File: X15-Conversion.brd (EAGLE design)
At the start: 50.8 x 62.9 mm, 31 parts, among them U1 LINEAR,AZ1117CR-3.3TRG1DIODES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

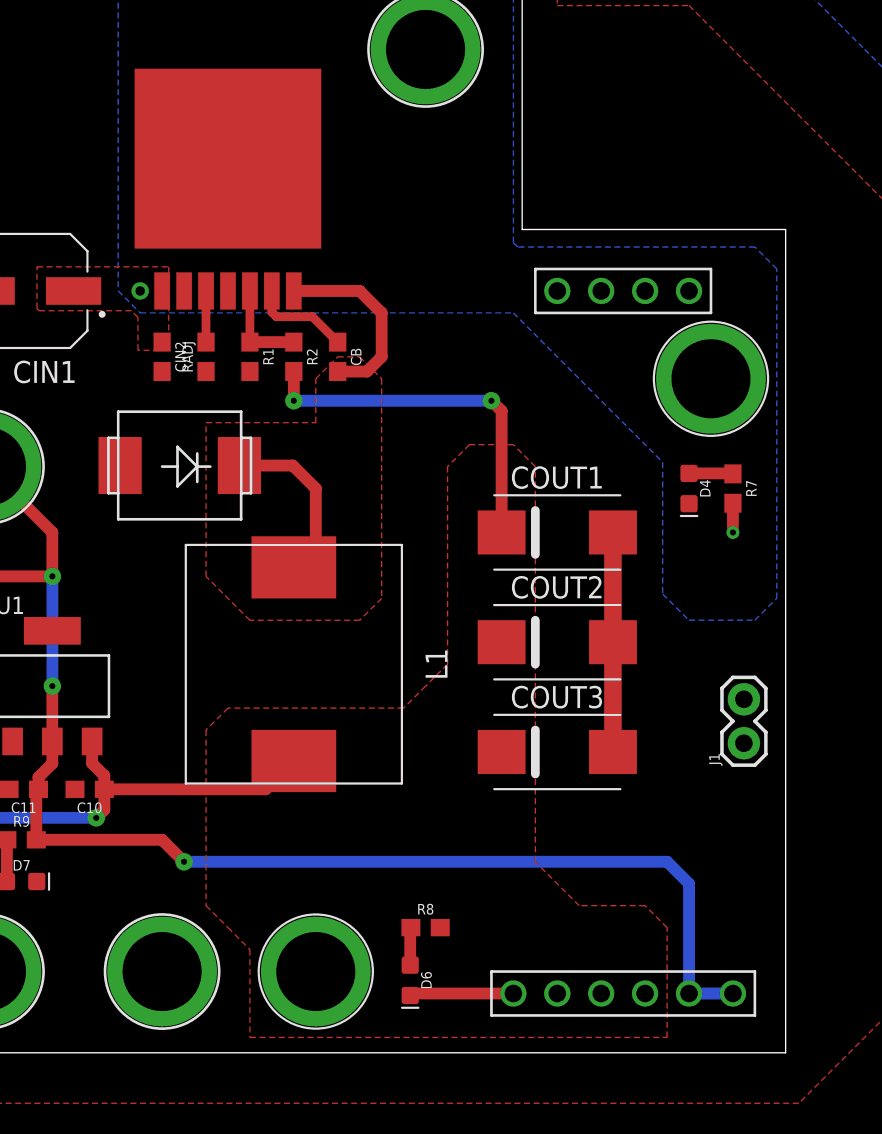
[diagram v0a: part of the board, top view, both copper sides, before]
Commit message: Changed the fonts
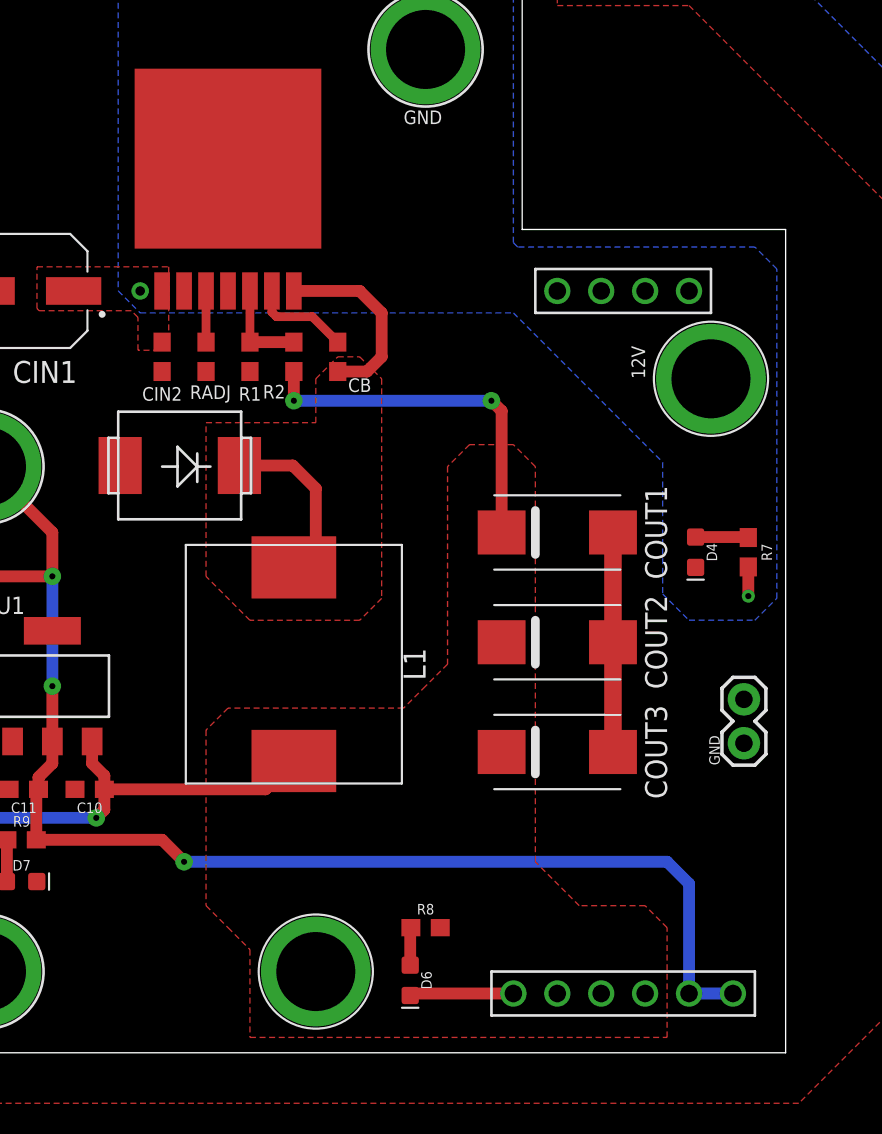
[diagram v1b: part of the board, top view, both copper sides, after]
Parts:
- removed U$13: GND_TESTPOINT, X15-Conversion-Parts-Library:GND_TESTPOINT
- moved U$11 10.2 mm to (5.08, 5.08)
- moved R7 3.79 mm to (49.1, 29.3)
- moved D4 3.70 mm to (46.1, 29.3)
- renumbered J1 to GND
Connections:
- net GND: no longer U$13.GND
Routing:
- net N$8: track 2.55 -> 3.06 mm
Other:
- board text added: "12V"
- board text added: "GND"

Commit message: Changed some wires
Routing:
- net BOOST: track 5.75 -> 6.35 mm
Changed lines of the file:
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@@
 <wire x1="11.899" y1="16.411" x2="11.19" y2="17.12" width="0.6858" layer="1"/>
 <wire x1="11.19" y1="17.12" x2="11.19" y2="18.39" width="0.6858" layer="1"/>
-<wire x1="11.899" y1="15.621" x2="21.221" y2="15.621" width="0.6858" layer="1"/>
-<wire x1="21.221" y1="15.621" x2="22.86" y2="17.26" width="0.6858" layer="1"/>
+<wire x1="22.491" y1="16.891" x2="15.709" y2="16.891" width="0.6858" layer="1"/>
+<wire x1="15.709" y1="16.891" x2="14.439" y2="15.621" width="0.6858" layer="1"/>
+<wire x1="14.439" y1="15.621" x2="11.899" y2="15.621" width="0.6858" layer="1"/>
+<wire x1="22.491" y1="16.891" x2="22.86" y2="17.26" width="0.6858" layer="1"/>
 <contactref element="J3" pad="2"/>
 <contactref element="J3" pad="1"/>
@@
 <contactref element="R9" pad="2"/>
 <contactref element="U1" pad="2"/>
-<wire x1="15.24" y1="12.7" x2="16.51" y2="11.43" width="0.6858" layer="1"/>
-<wire x1="15.24" y1="12.7" x2="7.962" y2="12.7" width="0.6858" layer="1"/>
+<wire x1="13.97" y1="11.43" x2="16.51" y2="11.43" width="0.6858" layer="1"/>
+<wire x1="13.97" y1="11.43" x2="12.7" y2="12.7" width="0.6858" layer="1"/>
+<wire x1="12.7" y1="12.7" x2="7.962" y2="12.7" width="0.6858" layer="1"/>
 <via x="16.51" y="11.43" extent="1-16" drill="0.35" diameter="1.016"/>
 <wire x1="16.51" y1="11.43" x2="44.45" y2="11.43" width="0.6858" layer="16"/>
@@
 <wire x1="21.59" y1="44.45" x2="21.59" y2="43.2292625" width="0.508" layer="1"/>
 <wire x1="21.8556625" y1="42.9636" x2="21.59" y2="43.2292625" width="0.508" layer="1"/>
-<wire x1="23.9264" y1="42.9636" x2="25.4" y2="41.49" width="0.508" layer="1"/>
-<wire x1="21.8556625" y1="42.9636" x2="23.9264" y2="42.9636" width="0.508" layer="1"/>
+<wire x1="25.4" y1="42.506" x2="24.9424" y2="42.9636" width="0.508" layer="1"/>
+<wire x1="25.4" y1="42.506" x2="25.4" y2="41.49" width="0.508" layer="1"/>
+<wire x1="21.8556625" y1="42.9636" x2="24.9424" y2="42.9636" width="0.508" layer="1"/>
 </signal>
 <signal name="FB">

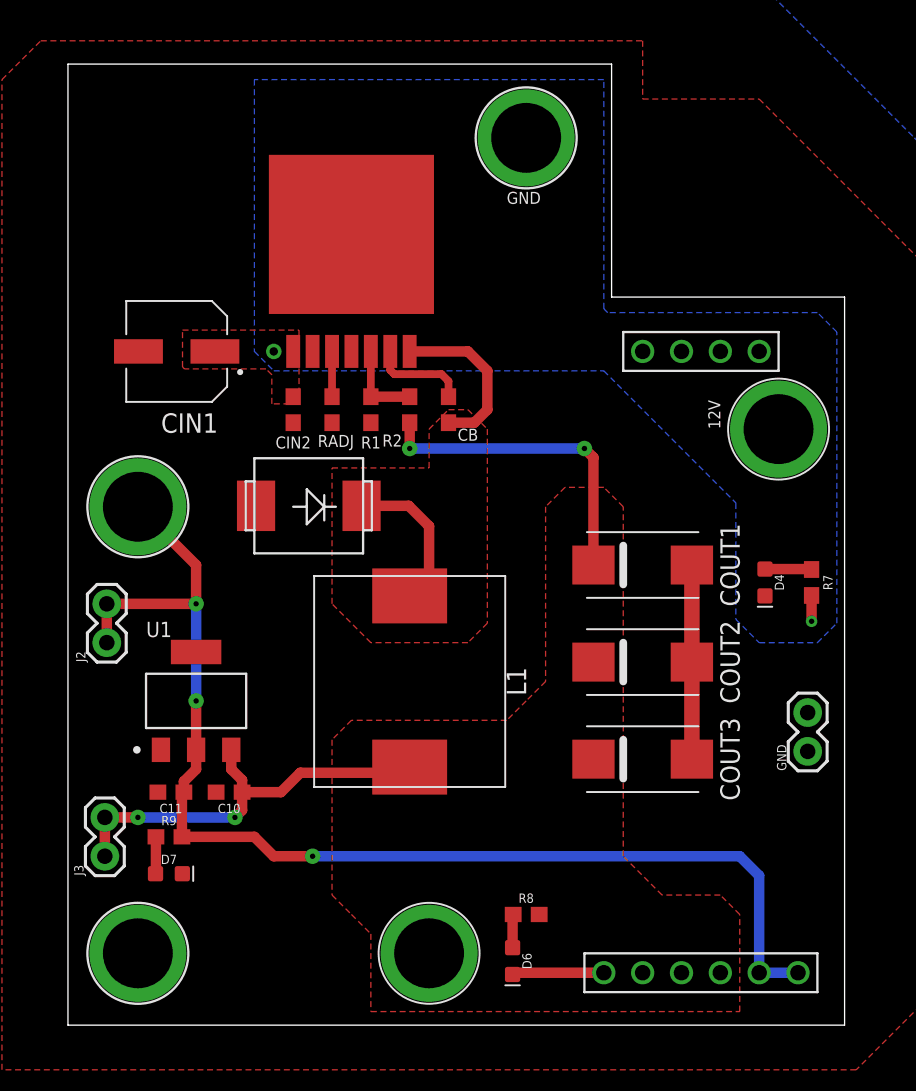
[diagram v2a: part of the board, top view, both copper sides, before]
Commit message: Added vias to ground
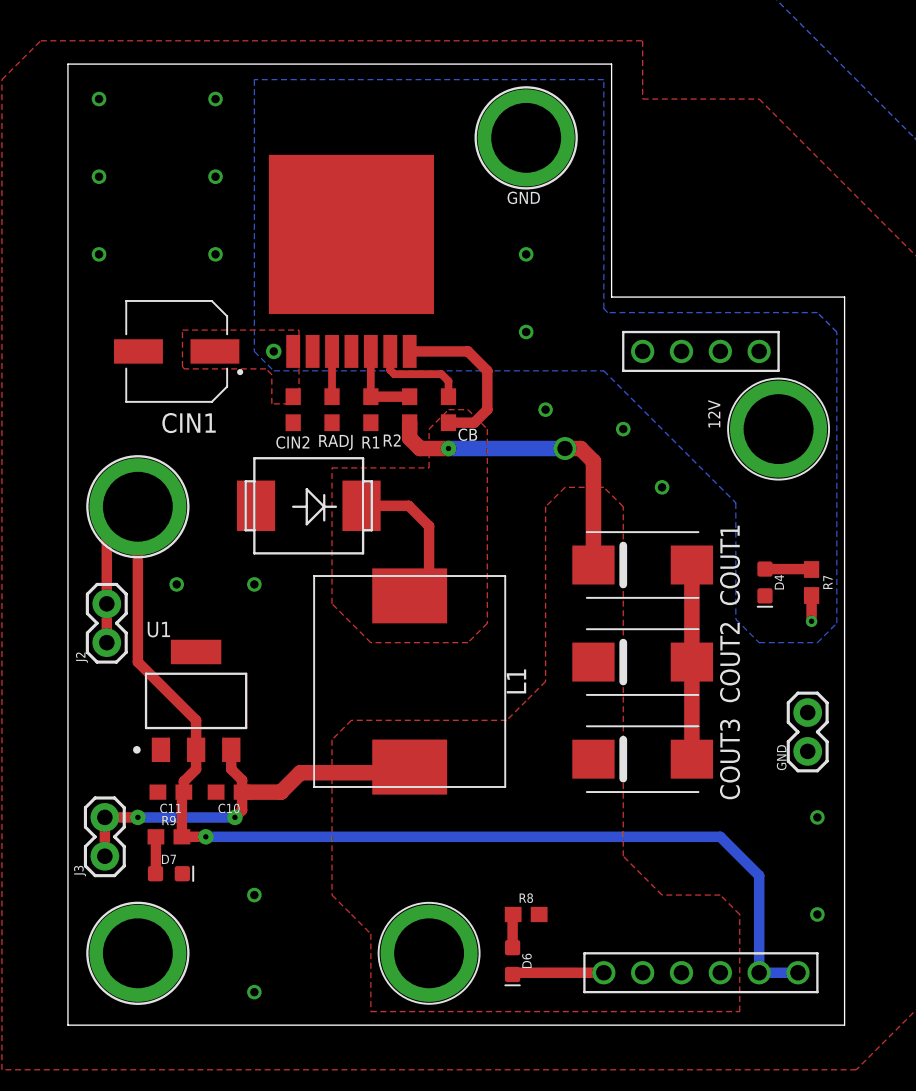
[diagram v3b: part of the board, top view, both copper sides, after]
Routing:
- net 3.3V: track 79.6 -> 81.0 mm, vias 3 -> 1
- net 5.2V: track 48.6 -> 48.0 mm
- net GND: vias 0 -> 17
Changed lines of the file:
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@@
 <vertex x="-10.16" y="63.5"/>
 </polygon>
+<via x="2.54" y="60.96" extent="1-16" drill="0.55"/>
+<via x="30.48" y="50.8" extent="1-16" drill="0.55"/>
+<via x="30.48" y="45.72" extent="1-16" drill="0.55"/>
+<via x="31.75" y="40.64" extent="1-16" drill="0.55"/>
+<via x="2.54" y="55.88" extent="1-16" drill="0.55"/>
+<via x="2.54" y="50.8" extent="1-16" drill="0.55"/>
+<via x="10.16" y="60.96" extent="1-16" drill="0.55"/>
+<via x="10.16" y="55.88" extent="1-16" drill="0.55"/>
+<via x="10.16" y="50.8" extent="1-16" drill="0.55"/>
+<via x="7.62" y="29.21" extent="1-16" drill="0.55"/>
+<via x="12.7" y="29.21" extent="1-16" drill="0.55"/>
+<via x="12.7" y="8.89" extent="1-16" drill="0.55"/>
+<via x="12.7" y="2.54" extent="1-16" drill="0.55"/>
+<via x="49.53" y="7.62" extent="1-16" drill="0.55"/>
+<via x="49.53" y="13.97" extent="1-16" drill="0.55"/>
+<via x="39.37" y="35.56" extent="1-16" drill="0.55"/>
+<via x="36.83" y="39.37" extent="1-16" drill="0.55"/>
 </signal>
 <signal name="5.2V">
@@
 <contactref element="COUT3" pad="+"/>
 <contactref element="L1" pad="2"/>
-<wire x1="34.88" y1="30.48" x2="34.88" y2="37.51" width="0.6858" layer="1"/>
-<wire x1="34.88" y1="37.51" x2="34.29" y2="38.1" width="0.6858" layer="1"/>
-<via x="34.29" y="38.1" extent="1-16" drill="0.35" diameter="1.016"/>
-<wire x1="22.86" y1="39.79" x2="22.86" y2="38.1" width="0.6858" layer="1"/>
-<via x="22.86" y="38.1" extent="1-16" drill="0.35" diameter="1.016"/>
-<wire x1="22.86" y1="38.1" x2="34.29" y2="38.1" width="0.6858" layer="16"/>
+<wire x1="34.88" y1="30.48" x2="34.88" y2="37.256" width="1.016" layer="1"/>
+<wire x1="34.88" y1="37.256" x2="34.036" y2="38.1" width="1.016" layer="1"/>
+<wire x1="34.036" y1="38.1" x2="33.02" y2="38.1" width="1.016" layer="1"/>
+<via x="33.02" y="38.1" extent="1-16" drill="1" diameter="1.016"/>
+<wire x1="23.534" y1="38.1" x2="22.86" y2="38.774" width="1.016" layer="1"/>
+<wire x1="22.86" y1="39.79" x2="22.86" y2="38.774" width="1.016" layer="1"/>
+<wire x1="25.4" y1="38.1" x2="23.534" y2="38.1" width="1.016" layer="1"/>
+<via x="25.4" y="38.1" extent="1-16" drill="0.35" diameter="1.016"/>
+<wire x1="25.4" y1="38.1" x2="33.02" y2="38.1" width="1.016" layer="16"/>
 <polygon width="0.2032" layer="1">
 <vertex x="33.02" y="35.56"/>
@@
 <wire x1="11.899" y1="16.411" x2="11.19" y2="17.12" width="0.6858" layer="1"/>
 <wire x1="11.19" y1="17.12" x2="11.19" y2="18.39" width="0.6858" layer="1"/>
-<wire x1="22.491" y1="16.891" x2="15.709" y2="16.891" width="0.6858" layer="1"/>
-<wire x1="15.709" y1="16.891" x2="14.439" y2="15.621" width="0.6858" layer="1"/>
-<wire x1="14.439" y1="15.621" x2="11.899" y2="15.621" width="0.6858" layer="1"/>
+<wire x1="22.491" y1="16.891" x2="15.709" y2="16.891" width="1.016" layer="1"/>
+<wire x1="15.709" y1="16.891" x2="14.439" y2="15.621" width="1.016" layer="1"/>
+<wire x1="14.439" y1="15.621" x2="11.899" y2="15.621" width="1.016" layer="1"/>
 <wire x1="22.491" y1="16.891" x2="22.86" y2="17.26" width="0.6858" layer="1"/>
 <contactref element="J3" pad="2"/>
@@
 <contactref element="R9" pad="2"/>
 <contactref element="U1" pad="2"/>
-<wire x1="13.97" y1="11.43" x2="16.51" y2="11.43" width="0.6858" layer="1"/>
-<wire x1="13.97" y1="11.43" x2="12.7" y2="12.7" width="0.6858" layer="1"/>
-<wire x1="12.7" y1="12.7" x2="7.962" y2="12.7" width="0.6858" layer="1"/>
-<via x="16.51" y="11.43" extent="1-16" drill="0.35" diameter="1.016"/>
-<wire x1="16.51" y1="11.43" x2="44.45" y2="11.43" width="0.6858" layer="16"/>
-<wire x1="44.45" y1="11.43" x2="45.72" y2="10.16" width="0.6858" layer="16"/>
+<wire x1="9.525" y1="12.7" x2="7.962" y2="12.7" width="0.6858" layer="1"/>
+<via x="9.525" y="12.7" extent="1-16" drill="0.35" diameter="1.016"/>
+<wire x1="43.18" y1="12.7" x2="9.525" y2="12.7" width="0.6858" layer="16"/>
+<wire x1="43.18" y1="12.7" x2="45.72" y2="10.16" width="0.6858" layer="16"/>
 <wire x1="45.72" y1="10.16" x2="45.72" y2="3.81" width="0.6858" layer="16"/>
 <wire x1="45.72" y1="3.81" x2="48.26" y2="3.81" width="0.6858" layer="16"/>
@@
 <wire x1="8.89" y1="17.12" x2="8.089" y2="16.319" width="0.6858" layer="1"/>
 <wire x1="8.89" y1="17.12" x2="8.89" y2="18.39" width="0.6858" layer="1"/>
-<wire x1="5.08" y1="34.29" x2="8.89" y2="30.48" width="0.6858" layer="1"/>
-<wire x1="8.89" y1="30.48" x2="8.89" y2="27.94" width="0.6858" layer="1"/>
-<via x="8.89" y="27.94" extent="1-16" drill="0.35" diameter="1.016"/>
-<wire x1="8.89" y1="27.94" x2="8.89" y2="21.59" width="0.6858" layer="16"/>
-<via x="8.89" y="21.59" extent="1-16" drill="0.35" diameter="1.016"/>
-<wire x1="8.89" y1="21.59" x2="8.89" y2="18.39" width="0.6858" layer="1"/>
+<wire x1="5.08" y1="34.29" x2="5.08" y2="24.13" width="0.6858" layer="1"/>
+<wire x1="5.08" y1="24.13" x2="8.89" y2="20.32" width="0.6858" layer="1"/>
 <contactref element="J2" pad="2"/>
 <contactref element="J2" pad="1"/>
 <wire x1="3.048" y1="25.4" x2="3.048" y2="27.94" width="0.6858" layer="1"/>
-<wire x1="3.048" y1="27.94" x2="8.89" y2="27.94" width="0.6858" layer="1"/>
+<wire x1="3.048" y1="27.94" x2="3.048" y2="32.258" width="0.6858" layer="1"/>
+<wire x1="3.048" y1="32.258" x2="5.08" y2="34.29" width="0.6858" layer="1"/>
+<wire x1="8.89" y1="20.32" x2="8.89" y2="18.39" width="0.6858" layer="1"/>
 </signal>
 <signal name="CRADJ">
